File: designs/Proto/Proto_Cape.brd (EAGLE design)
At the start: 71.8 x 58.4 mm, 24 parts

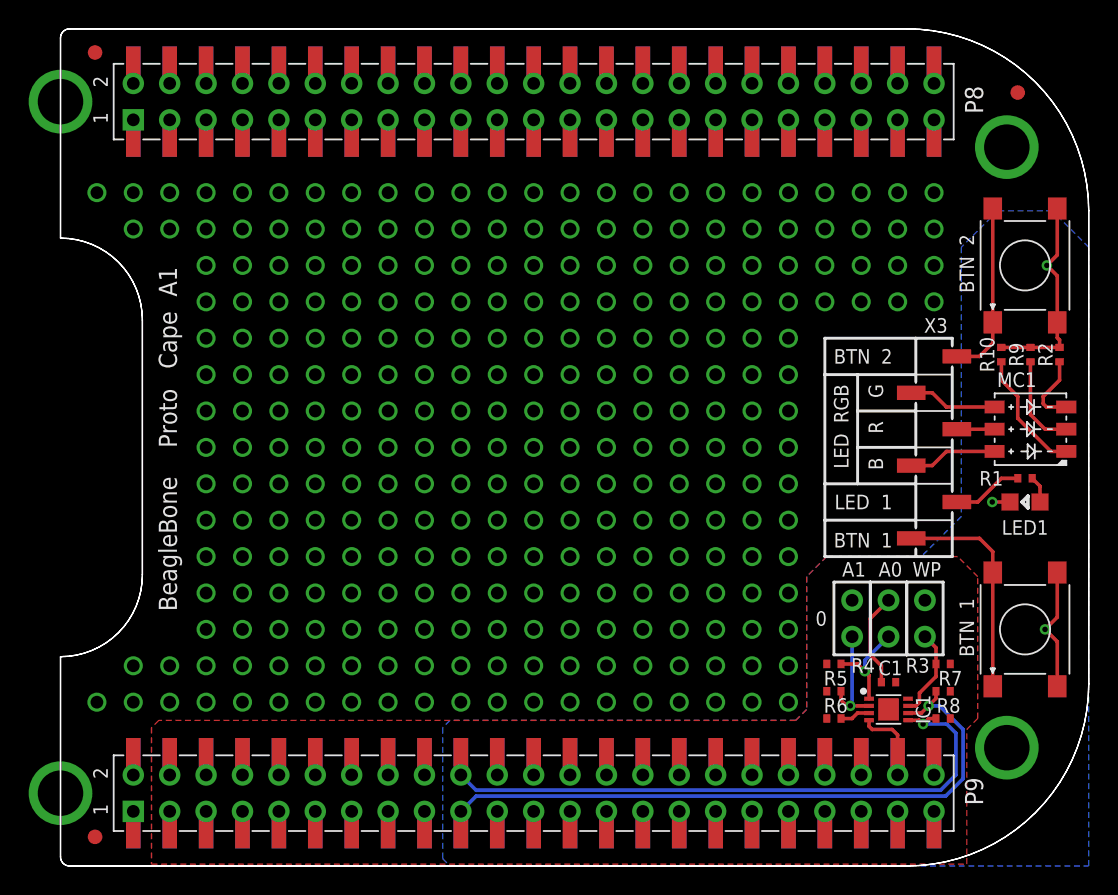
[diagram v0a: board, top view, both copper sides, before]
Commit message: Added the revised EAGLE schematics. Also removed two files that were probably not intended to be added as they are lock files in EAGLE.
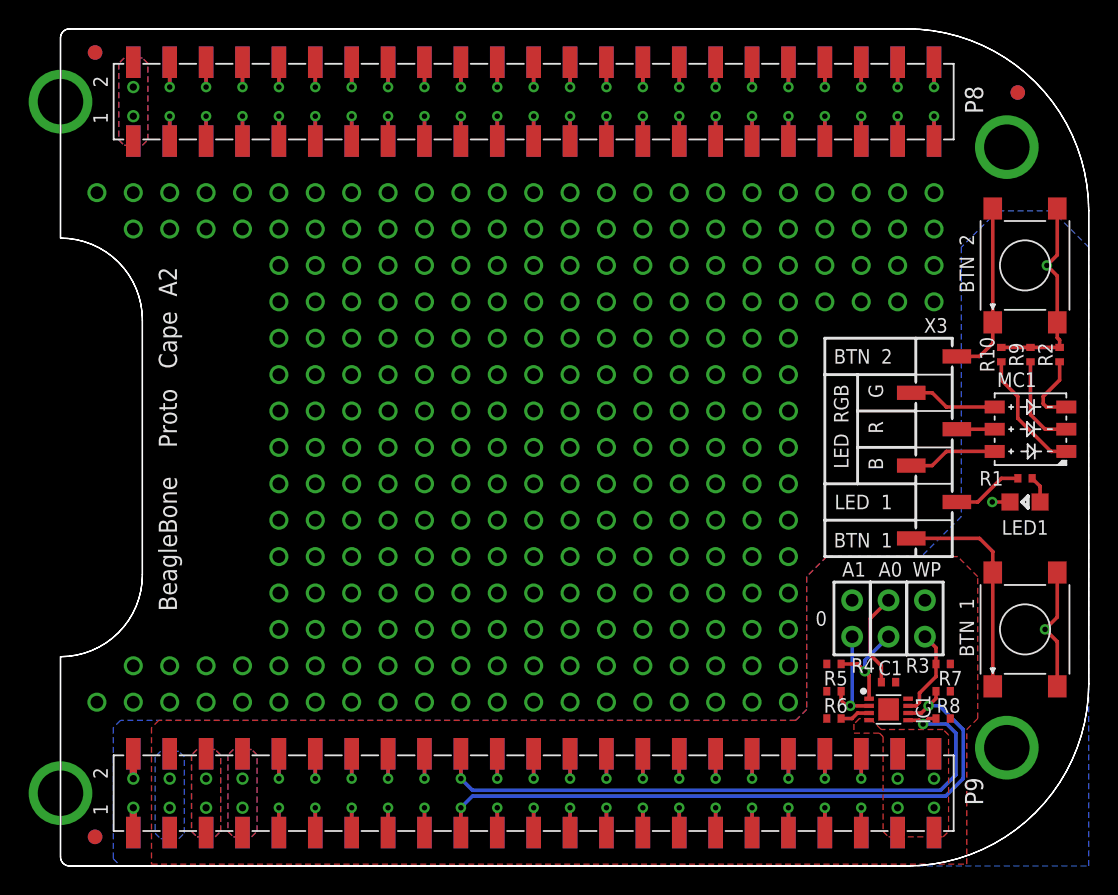
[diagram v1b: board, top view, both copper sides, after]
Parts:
- added FUD4, FUD5, FUD6: FIDUCIAL, GHI:FIDUCIAL_40MIL
- BB.CAPE1: value BEAGLEBONE.CAPE.TOP/BOTTOM-PADS/W/TH -> BEAGLEBONE.CAPE.TOP/BOTTOM-PADS; device GHI-Solutions:BEAGLEBONE.CAPE.TOP/BOTTOM-PADS.W/TH -> GHI-Solutions:BEAGLEBONE.CAPE.TOP/BOTTOM-PADS
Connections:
- new net +5V: BB.CAPE1.B9.7, BB.CAPE1.B9.8, BB.CAPE1.T9.7, BB.CAPE1.T9.8
- new net COMMON.GND: BB.CAPE1.B8.1, BB.CAPE1.B8.2, BB.CAPE1.T8.1, BB.CAPE1.T8.2
- new net P8.10: BB.CAPE1.B8.10, BB.CAPE1.T8.10
- new net P8.11: BB.CAPE1.B8.11, BB.CAPE1.T8.11
- new net P8.12: BB.CAPE1.B8.12, BB.CAPE1.T8.12
- new net P8.13: BB.CAPE1.B8.13, BB.CAPE1.T8.13
- new net P8.14: BB.CAPE1.B8.14, BB.CAPE1.T8.14
- new net P8.15: BB.CAPE1.B8.15, BB.CAPE1.T8.15
- new net P8.16: BB.CAPE1.B8.16, BB.CAPE1.T8.16
- new net P8.17: BB.CAPE1.B8.17, BB.CAPE1.T8.17
- new net P8.18: BB.CAPE1.B8.18, BB.CAPE1.T8.18
- new net P8.19: BB.CAPE1.B8.19, BB.CAPE1.T8.19
- new net P8.20: BB.CAPE1.B8.20, BB.CAPE1.T8.20
- new net P8.21: BB.CAPE1.B8.21, BB.CAPE1.T8.21
- new net P8.22: BB.CAPE1.B8.22, BB.CAPE1.T8.22
- new net P8.23: BB.CAPE1.B8.23, BB.CAPE1.T8.23
- new net P8.24: BB.CAPE1.B8.24, BB.CAPE1.T8.24
- new net P8.25: BB.CAPE1.B8.25, BB.CAPE1.T8.25
- new net P8.26: BB.CAPE1.B8.26, BB.CAPE1.T8.26
- new net P8.27: BB.CAPE1.B8.27, BB.CAPE1.T8.27
- new net P8.28: BB.CAPE1.B8.28, BB.CAPE1.T8.28
- new net P8.29: BB.CAPE1.B8.29, BB.CAPE1.T8.29
- new net P8.3: BB.CAPE1.B8.3, BB.CAPE1.T8.3
- new net P8.30: BB.CAPE1.B8.30, BB.CAPE1.T8.30
- new net P8.31: BB.CAPE1.B8.31, BB.CAPE1.T8.31
- new net P8.32: BB.CAPE1.B8.32, BB.CAPE1.T8.32
- new net P8.33: BB.CAPE1.B8.33, BB.CAPE1.T8.33
- new net P8.34: BB.CAPE1.B8.34, BB.CAPE1.T8.34
- new net P8.35: BB.CAPE1.B8.35, BB.CAPE1.T8.35
- new net P8.36: BB.CAPE1.B8.36, BB.CAPE1.T8.36
- new net P8.37: BB.CAPE1.B8.37, BB.CAPE1.T8.37
- new net P8.38: BB.CAPE1.B8.38, BB.CAPE1.T8.38
- new net P8.39: BB.CAPE1.B8.39, BB.CAPE1.T8.39
- new net P8.4: BB.CAPE1.B8.4, BB.CAPE1.T8.4
- new net P8.40: BB.CAPE1.B8.40, BB.CAPE1.T8.40
- new net P8.41: BB.CAPE1.B8.41, BB.CAPE1.T8.41
- new net P8.42: BB.CAPE1.B8.42, BB.CAPE1.T8.42
- new net P8.43: BB.CAPE1.B8.43, BB.CAPE1.T8.43
- new net P8.44: BB.CAPE1.B8.44, BB.CAPE1.T8.44
- new net P8.45: BB.CAPE1.B8.45, BB.CAPE1.T8.45
- new net P8.46: BB.CAPE1.B8.46, BB.CAPE1.T8.46
- new net P8.5: BB.CAPE1.B8.5, BB.CAPE1.T8.5
- new net P8.6: BB.CAPE1.B8.6, BB.CAPE1.T8.6
- new net P8.7: BB.CAPE1.B8.7, BB.CAPE1.T8.7
- new net P8.8: BB.CAPE1.B8.8, BB.CAPE1.T8.8
- new net P8.9: BB.CAPE1.B8.9, BB.CAPE1.T8.9
- new net P9.10: BB.CAPE1.B9.10, BB.CAPE1.T9.10
- new net P9.11: BB.CAPE1.B9.11, BB.CAPE1.T9.11
- new net P9.12: BB.CAPE1.B9.12, BB.CAPE1.T9.12
- new net P9.13: BB.CAPE1.B9.13, BB.CAPE1.T9.13
- new net P9.14: BB.CAPE1.B9.14, BB.CAPE1.T9.14
- new net P9.15: BB.CAPE1.B9.15, BB.CAPE1.T9.15
- new net P9.16: BB.CAPE1.B9.16, BB.CAPE1.T9.16
- new net P9.17: BB.CAPE1.B9.17, BB.CAPE1.T9.17
- new net P9.18: BB.CAPE1.B9.18, BB.CAPE1.T9.18
- new net P9.21: BB.CAPE1.B9.21, BB.CAPE1.T9.21
- new net P9.22: BB.CAPE1.B9.22, BB.CAPE1.T9.22
- new net P9.23: BB.CAPE1.B9.23, BB.CAPE1.T9.23
- new net P9.24: BB.CAPE1.B9.24, BB.CAPE1.T9.24
- new net P9.25: BB.CAPE1.B9.25, BB.CAPE1.T9.25
- new net P9.26: BB.CAPE1.B9.26, BB.CAPE1.T9.26
- new net P9.27: BB.CAPE1.B9.27, BB.CAPE1.T9.27
- new net P9.28: BB.CAPE1.B9.28, BB.CAPE1.T9.28
- new net P9.29: BB.CAPE1.B9.29, BB.CAPE1.T9.29
- new net P9.30: BB.CAPE1.B9.30, BB.CAPE1.T9.30
- new net P9.31: BB.CAPE1.B9.31, BB.CAPE1.T9.31
- new net P9.32: BB.CAPE1.B9.32, BB.CAPE1.T9.32
- new net P9.33: BB.CAPE1.B9.33, BB.CAPE1.T9.33
- new net P9.34: BB.CAPE1.B9.34, BB.CAPE1.T9.34
- new net P9.35: BB.CAPE1.B9.35, BB.CAPE1.T9.35
- new net P9.36: BB.CAPE1.B9.36, BB.CAPE1.T9.36
- new net P9.37: BB.CAPE1.B9.37, BB.CAPE1.T9.37
- new net P9.38: BB.CAPE1.B9.38, BB.CAPE1.T9.38
- new net P9.39: BB.CAPE1.B9.39, BB.CAPE1.T9.39
- new net P9.40: BB.CAPE1.B9.40, BB.CAPE1.T9.40
- new net P9.41: BB.CAPE1.B9.41, BB.CAPE1.T9.41
- new net P9.42: BB.CAPE1.B9.42, BB.CAPE1.T9.42
- new net P9.9: BB.CAPE1.B9.9, BB.CAPE1.T9.9
- new net VDD_5V: BB.CAPE1.B9.5, BB.CAPE1.B9.6, BB.CAPE1.T9.5, BB.CAPE1.T9.6
- net GND: now also BB.CAPE1.B9.1, BB.CAPE1.B9.2, BB.CAPE1.T9.1, BB.CAPE1.T9.2; no longer BB.CAPE1.P9.43, BB.CAPE1.P9.44, BB.CAPE1.P9.45, BB.CAPE1.P9.46
- net SCL: no longer BB.CAPE1.P9.19
- net SDA: no longer BB.CAPE1.P9.20
- net VCC: now also IC1.8; no longer BB.CAPE1.P9.3, BB.CAPE1.P9.4
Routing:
- net GND: track 46.7 -> 34.4 mm, vias 3 -> 9
- net P8.8: track 0.00 -> 3.47 mm, vias 0 -> 1
- net P8.6: track 0.00 -> 3.47 mm, vias 0 -> 1
- net P8.46: track 0.00 -> 3.47 mm, vias 0 -> 1
- net P8.44: track 0.00 -> 3.47 mm, vias 0 -> 1
- net P8.42: track 0.00 -> 3.47 mm, vias 0 -> 1
- net P8.40: track 0.00 -> 3.47 mm, vias 0 -> 1
- net P8.4: track 0.00 -> 3.47 mm, vias 0 -> 1
- net P8.38: track 0.00 -> 3.47 mm, vias 0 -> 1
- net P8.36: track 0.00 -> 3.47 mm, vias 0 -> 1
- net P8.34: track 0.00 -> 3.47 mm, vias 0 -> 1
- net P8.32: track 0.00 -> 3.47 mm, vias 0 -> 1
- net P8.30: track 0.00 -> 3.47 mm, vias 0 -> 1
- net P8.28: track 0.00 -> 3.47 mm, vias 0 -> 1
- net P8.26: track 0.00 -> 3.47 mm, vias 0 -> 1
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- added copper zone on layer 1, net +5V
- added copper zone on layer 16, net +5V
- added copper zone on layer 1, net COMMON.GND
- added copper zone on layer 16, net COMMON.GND
- added copper zone on layer 1, net GND
- added copper zone on layer 16, net VCC
- added copper zone on layer 1, net VDD_5V
- added copper zone on layer 16, net VDD_5V
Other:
- board text added: "A2"
